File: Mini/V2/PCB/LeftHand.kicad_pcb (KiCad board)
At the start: 2 copper layers, 155.9 x 99.3 mm, 30 parts

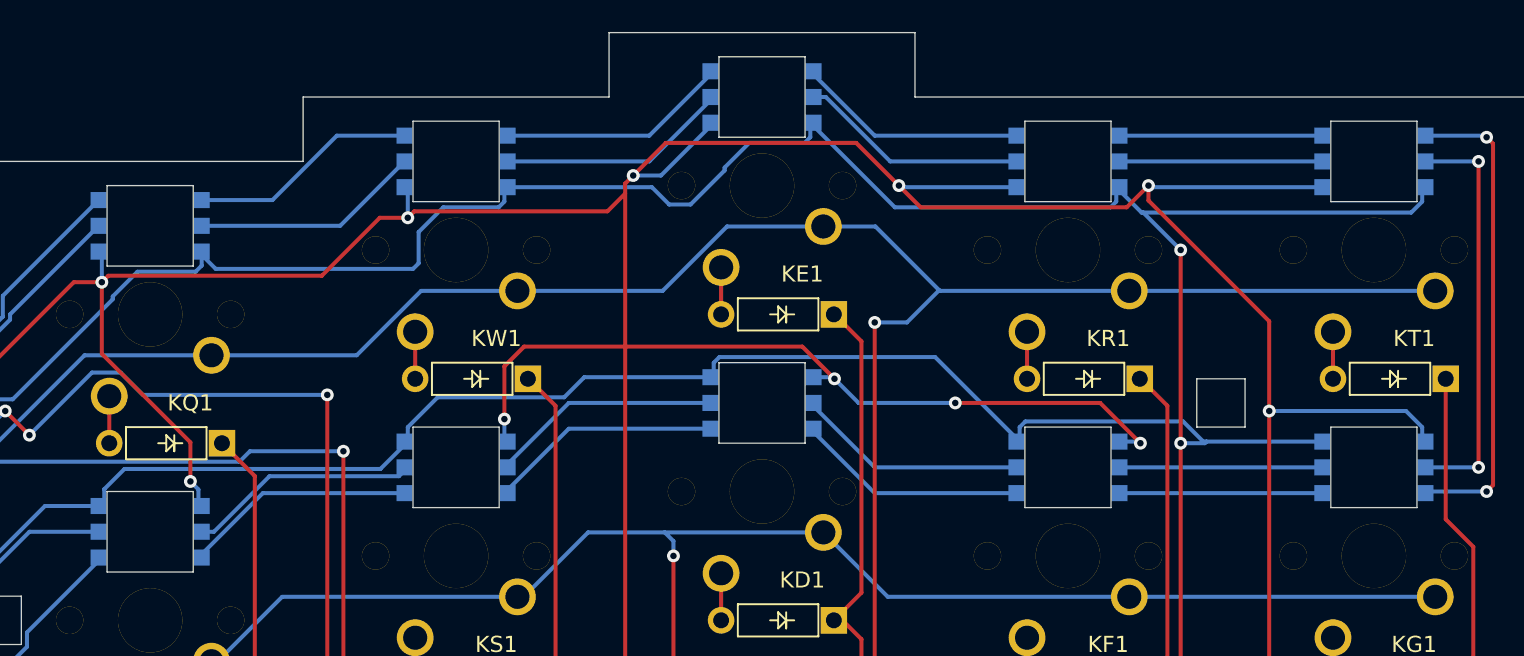
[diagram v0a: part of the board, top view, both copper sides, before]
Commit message: Fixing some more wires.
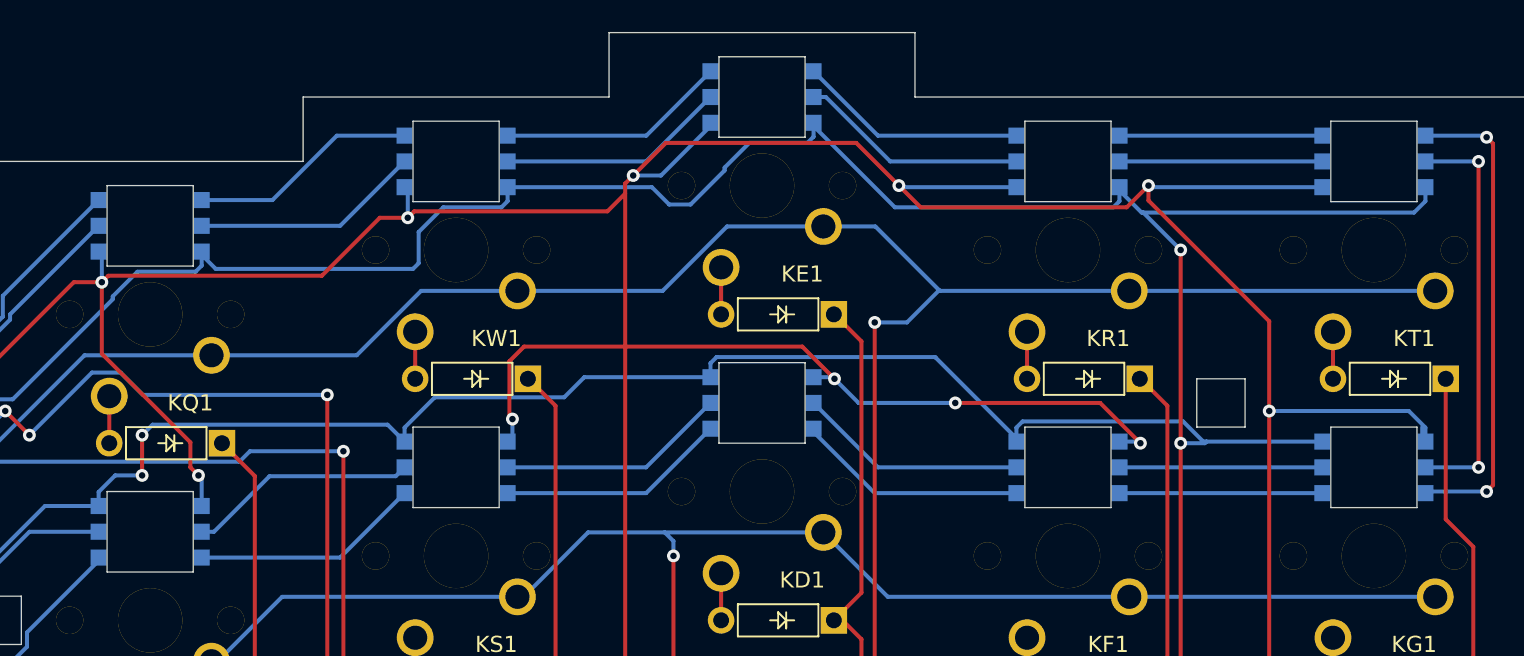
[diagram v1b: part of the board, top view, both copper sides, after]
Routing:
- net VCC: track 632.6 -> 636.2 mm, vias 14 -> 16
- net GND: track 631.6 -> 632.8 mm

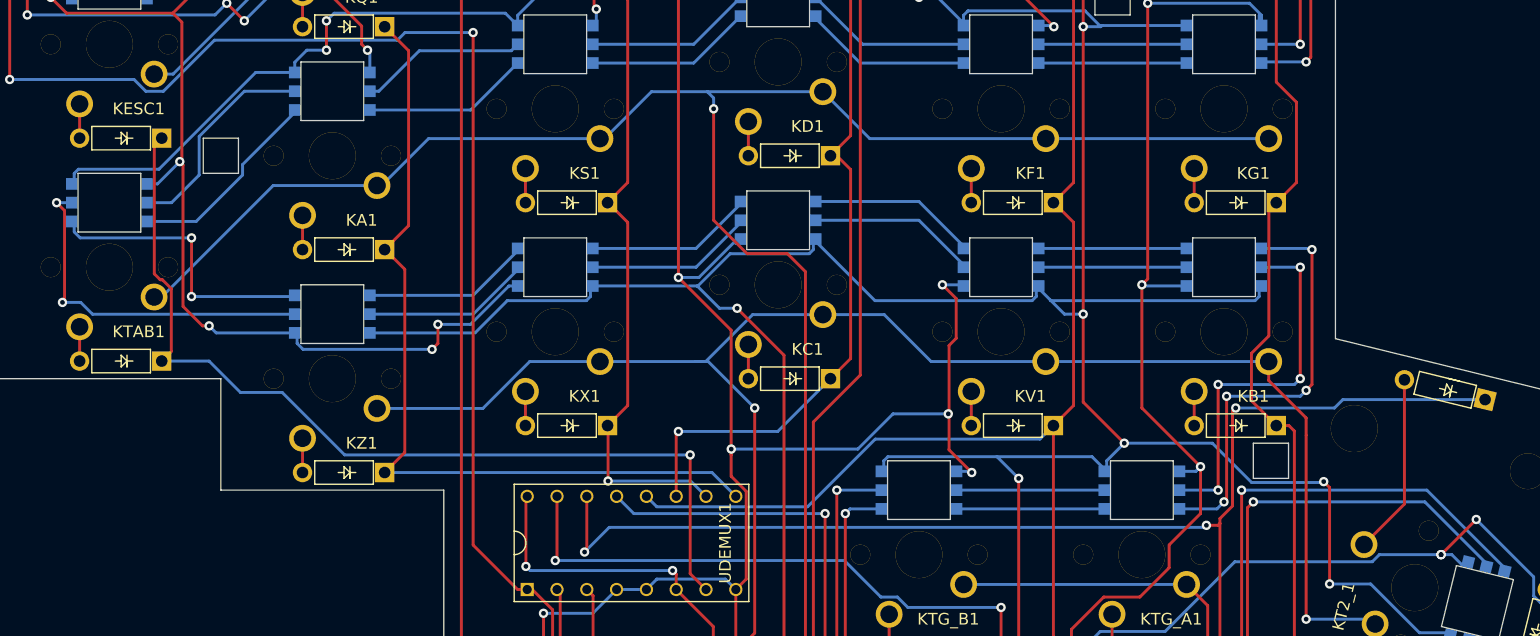
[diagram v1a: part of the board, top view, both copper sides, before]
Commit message: Finished fixing LED hole wiring adjustments.
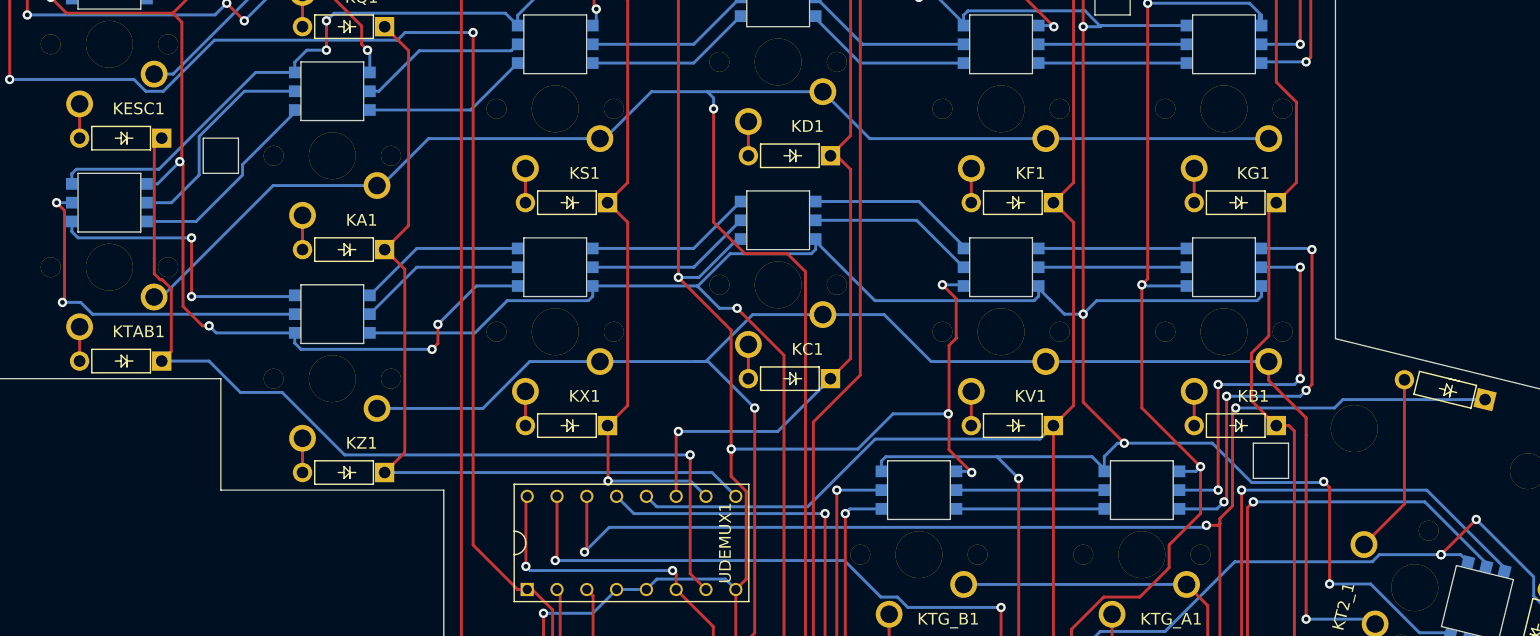
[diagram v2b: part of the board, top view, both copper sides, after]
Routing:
- net VCC: track 636.2 -> 635.1 mm

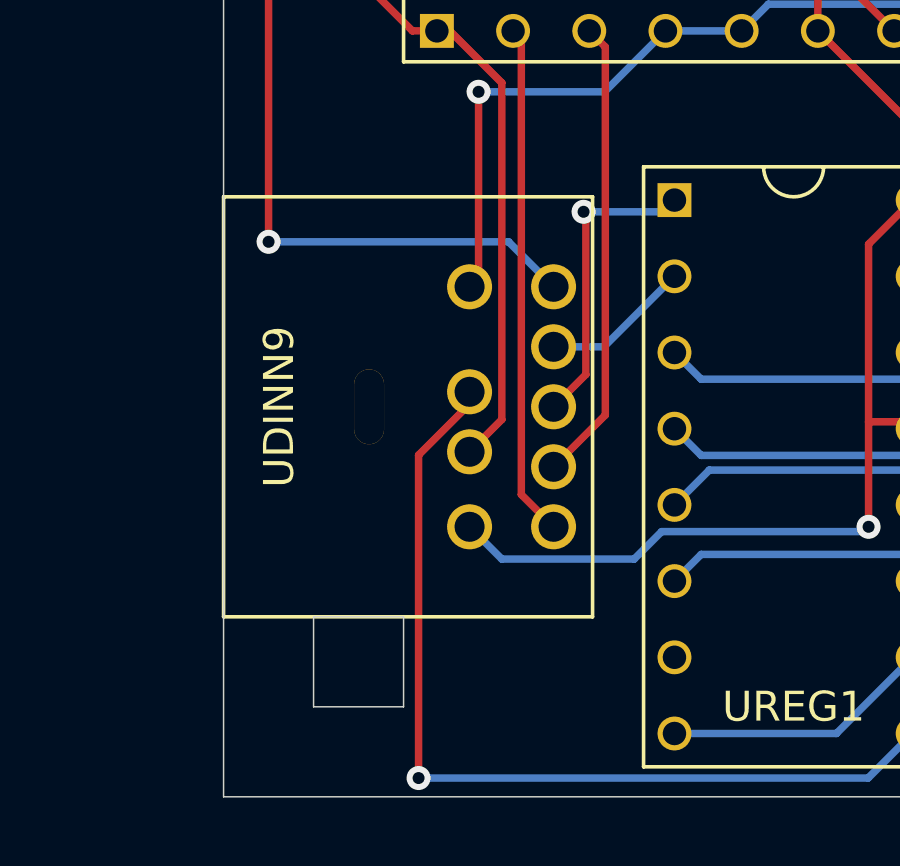
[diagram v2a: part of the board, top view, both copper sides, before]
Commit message: Moving connector up 0.5mm.
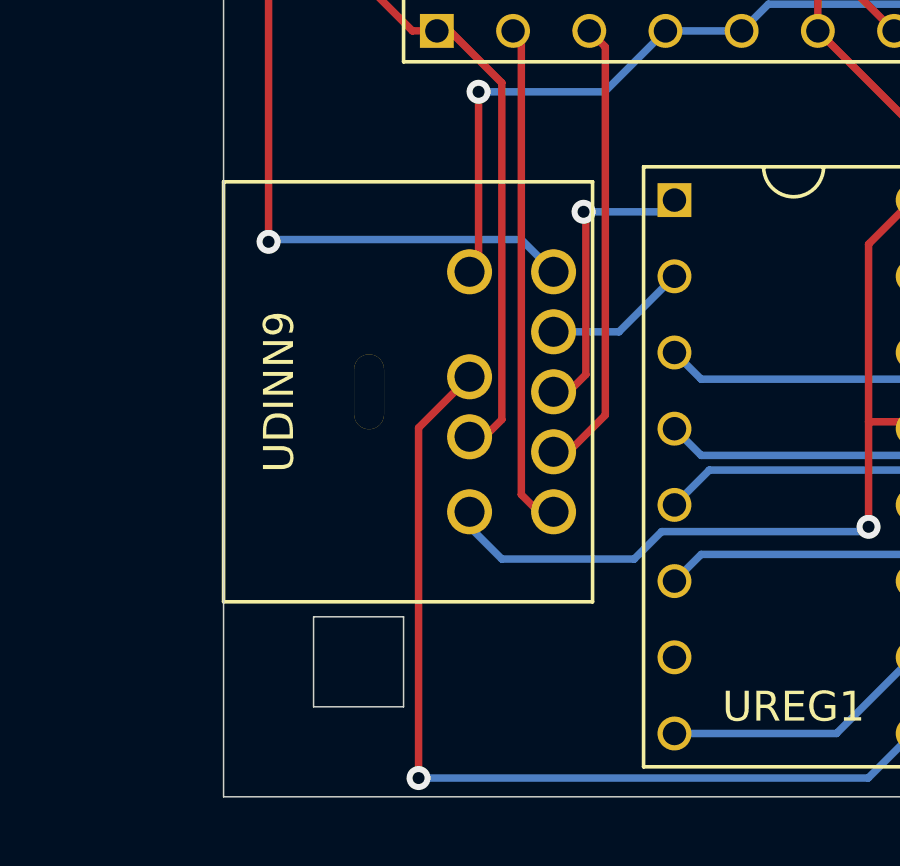
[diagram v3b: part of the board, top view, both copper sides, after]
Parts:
- moved UDINN9 0.50 mm to (54.9, 97.5)
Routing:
- net RX: track 30.7 -> 31.2 mm
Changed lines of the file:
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@@
   )
   (module Mini:MiniDin9 (layer F.Cu)
-    (at 54.85 98 270)
+    (at 54.85 97.5 270)
     (fp_text reference UDINN9 (at 0 3 90) (layer F.SilkS)
       (effects (font (size 1 1) (thickness 0.15)))
@@
   (segment (start 13 32) (end 18.4 32) (width 0.25) (layer B.Cu) (net 34))
   (via (at 51.5 92.5) (size 0.8) (drill 0.4) (layers F.Cu B.Cu) (net 35))
-  (segment (start 59.5 92.5) (end 51.5 92.5) (width 0.25) (layer B.Cu) (net 35))
-  (segment (start 61 94) (end 59.5 92.5) (width 0.25) (layer B.Cu) (net 35))
   (via (at 51.5 34.5) (size 0.8) (drill 0.4) (layers F.Cu B.Cu) (net 35))
   (segment (start 51.5 92.5) (end 51.5 34.5) (width 0.25) (layer F.Cu) (net 35))
@@
   (segment (start 18 34) (end 18.5 33.5) (width 0.25) (layer B.Cu) (net 35))
   (segment (start 14.5 34) (end 18 34) (width 0.25) (layer B.Cu) (net 35))
+  (segment (start 51.575001 92.424999) (end 51.5 92.5) (width 0.25) (layer B.Cu) (net 35))
+  (segment (start 59.924999 92.424999) (end 51.575001 92.424999) (width 0.25) (layer B.Cu) (net 35))
+  (segment (start 61 93.5) (end 59.924999 92.424999) (width 0.25) (layer B.Cu) (net 35))
   (segment (start 24.5 31.9) (end 29.094988 31.9) (width 0.25) (layer B.Cu) (net 36))
   (segment (start 31.35001 29.644978) (end 31.35001 28.34999) (width 0.25) (layer B.Cu) (net 36))
@@
   (segment (start 71.485 110.375) (end 56.5 110.375) (width 0.25) (layer B.Cu) (net 88))
   (segment (start 72.97 108.89) (end 71.485 110.375) (width 0.25) (layer B.Cu) (net 88))
-  (segment (start 58.2 97.908998) (end 58.2 97.5) (width 0.25) (layer F.Cu) (net 88))
-  (segment (start 56.5 99.608998) (end 58.2 97.908998) (width 0.25) (layer F.Cu) (net 88))
-  (segment (start 56.5 110.375) (end 56.5 99.608998) (width 0.25) (layer F.Cu) (net 88))
-  (segment (start 62.68 96) (end 65.03 93.65) (width 0.25) (layer B.Cu) (net 89))
-  (segment (start 61 96) (end 62.68 96) (width 0.25) (layer B.Cu) (net 89))
+  (segment (start 56.5 98.7) (end 58.2 97) (width 0.25) (layer F.Cu) (net 88))
+  (segment (start 56.5 110.375) (end 56.5 98.7) (width 0.25) (layer F.Cu) (net 88))
+  (segment (start 63.18 95.5) (end 65.03 93.65) (width 0.25) (layer B.Cu) (net 89))
+  (segment (start 61 95.5) (end 63.18 95.5) (width 0.25) (layer B.Cu) (net 89))
   (via (at 62 91.5) (size 0.8) (drill 0.4) (layers F.Cu B.Cu) (net 90))
   (segment (start 62.075001 91.575001) (end 62 91.5) (width 0.25) (layer F.Cu) (net 90))
